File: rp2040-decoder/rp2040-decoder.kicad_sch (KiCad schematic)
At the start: 58 parts, among them J4 5052702412, Q1 TPM2008, Q2 TPM2008, Q3 TPM2008, Q4 TPM2008, Q5 TPM2008, Q6 TPM2008, Q7 TPM2008, U1 W25Q64JVXGIQ, U2 AP63203WU, U3 RP2040, U4 MD9927, U5 MAX98357A, U6 LMV331, Y1 X252012MMB4SI

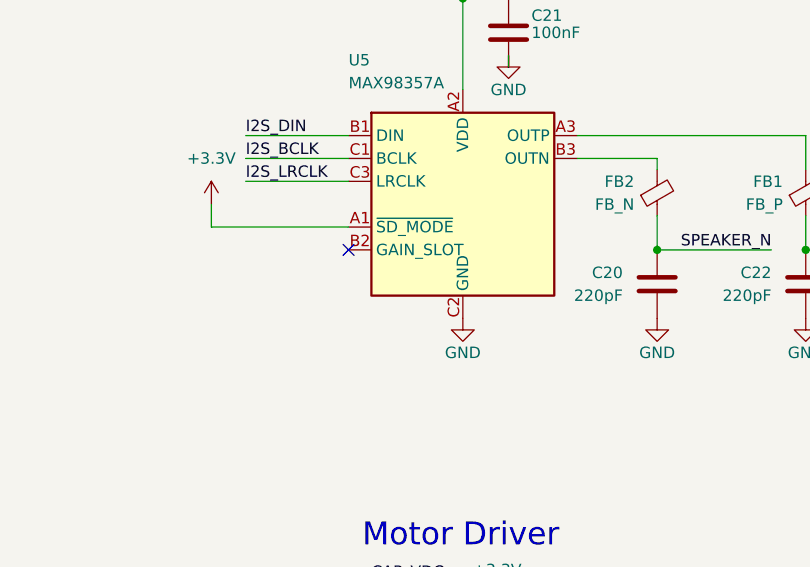
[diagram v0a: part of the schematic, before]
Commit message: fix: convert 0.2mm vias to 0.3mm
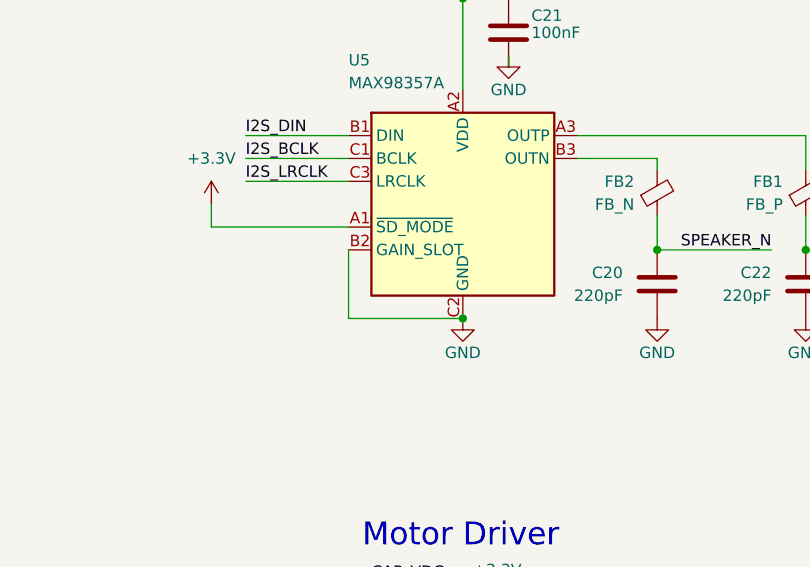
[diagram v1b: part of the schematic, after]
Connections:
- net GND: now also U5.B2 (GAIN_SLOT)
- no-connect marks 17 -> 16
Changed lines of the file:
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@@
+	)
+	(junction
+		(at 354.33 163.83)
+		(diameter 0)
+		(color 0 0 0 0)
 	)
 	(junction
@@
 	)
 	(no_connect
-		(at 341.63 156.21)
-	)
-	(no_connect
 		(at 237.49 217.17)
 	)
@@
 	(wire
 		(pts
+			(xy 341.63 163.83) (xy 354.33 163.83)
+		)
+		(stroke
+			(width 0)
+			(type default)
+		)
+	)
+	(wire
+		(pts
 			(xy 107.95 208.28) (xy 107.95 210.82)
 		)
@@
 		)
 		(stroke
+			(width 0)
+			(type default)
+		)
+	)
+	(wire
+		(pts
+			(xy 341.63 156.21) (xy 341.63 163.83)
+		)
+		(stroke

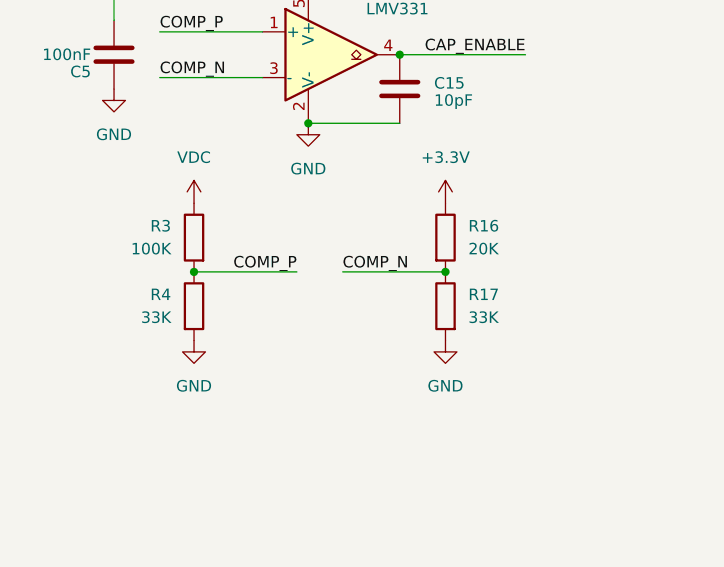
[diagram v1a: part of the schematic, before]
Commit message: fix: reduce unique part count
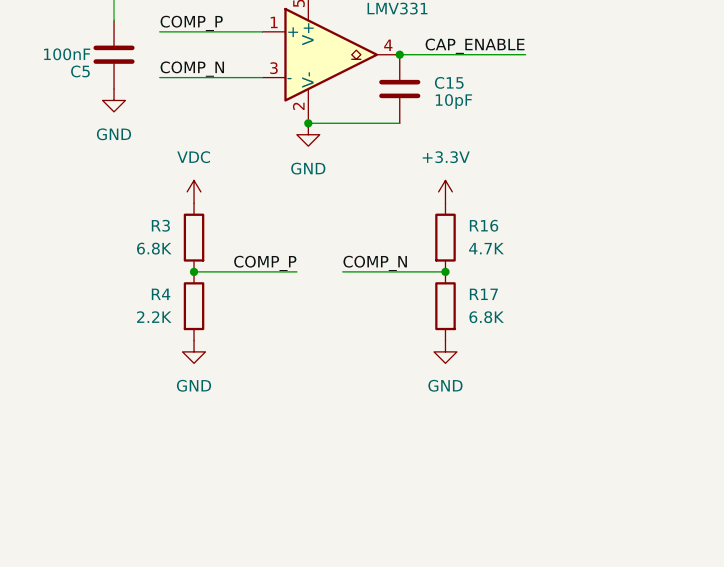
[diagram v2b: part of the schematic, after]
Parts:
- R16: value 20K -> 4.7K; LCSC C473466 -> C270346
- R17: value 33K -> 6.8K; LCSC C473534 -> C423451
- R3: value 100K -> 6.8K; LCSC C270364 -> C423451
- R4: value 33K -> 2.2K
- Y1: JLCPCB_CORRECTION (none) -> 0;0;180
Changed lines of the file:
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@@
 			)
 		)
-		(property "Value" "33K"
+		(property "Value" "2.2K"
 			(at 31.75 124.4599 0)
 			(effects
@@
 			)
 		)
-		(property "Value" "100K"
+		(property "Value" "6.8K"
 			(at 31.75 116.8399 0)
 			(effects
@@
 			)
 		)
-		(property "LCSC" "C270364"
+		(property "LCSC" "C423451"
 			(at 34.29 115.57 0)
 			(effects
@@
 			)
 		)
+		(property "JLCPCB_CORRECTION" "0;0;180"
+			(at 101.6 241.3 0)
+			(effects
+				(font
+					(size 1.27 1.27)
+				)
+				(hide yes)
+			)
+		)
 		(pin "1"
 		)
@@
 			)
 		)
-		(property "Value" "20K"
+		(property "Value" "4.7K"
 			(at 64.77 116.8399 0)
 			(effects
@@
 			)
 		)
-		(property "LCSC" "C473466"
+		(property "LCSC" "C270346"
 			(at 62.23 115.57 0)
 			(effects
@@
 			)
 		)
-		(property "Value" "33K"
+		(property "Value" "6.8K"
 			(at 64.77 124.4599 0)
 			(effects
@@
 			)
 		)
-		(property "LCSC" "C473534"
+		(property "LCSC" "C423451"
 			(at 62.23 123.19 0)
 			(effects
